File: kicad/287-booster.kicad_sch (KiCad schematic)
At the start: 4 parts

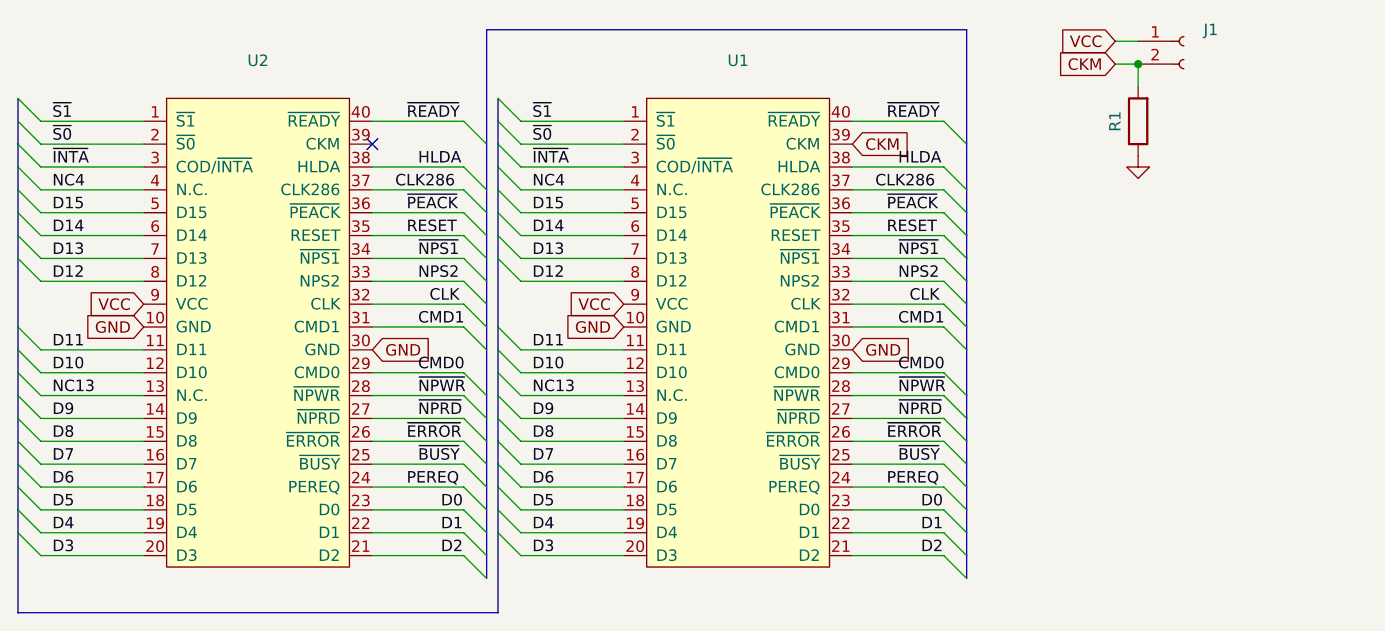
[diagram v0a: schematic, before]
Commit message: Switched to KiCad 7
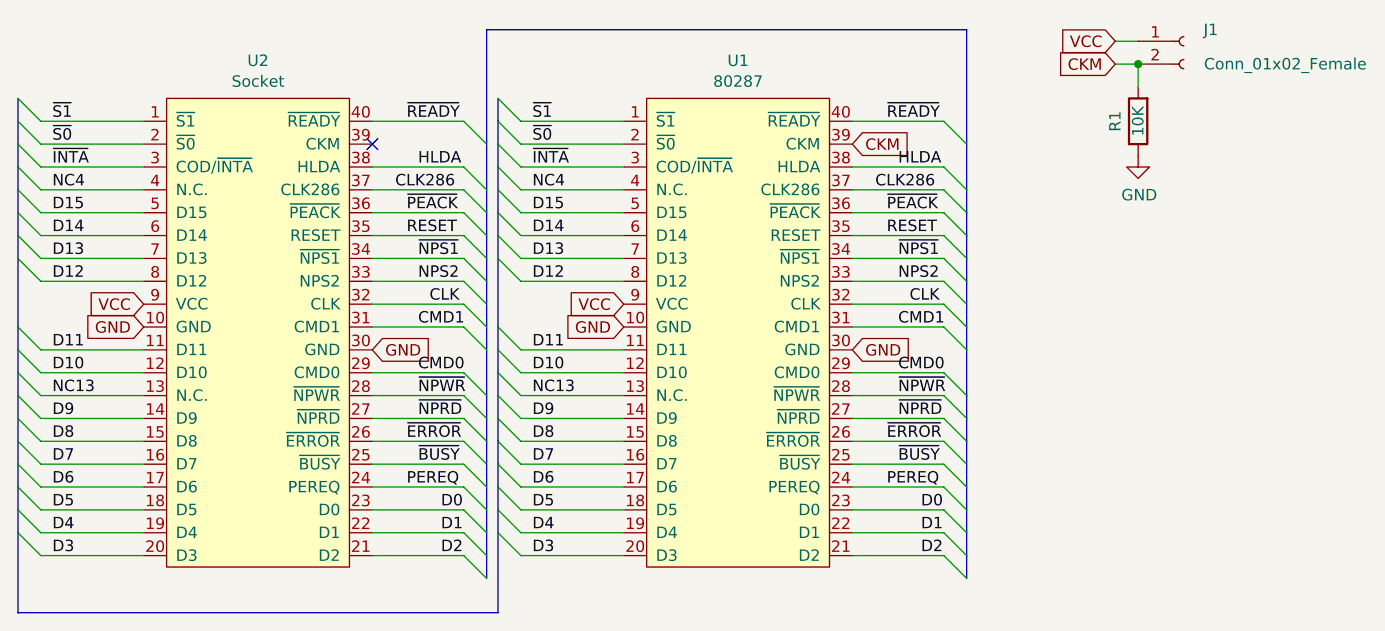
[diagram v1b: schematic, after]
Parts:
- J1: value (none) -> Conn_01x02_Female; footprint (none) -> Connector_PinHeader_2.54mm:PinHeader_1x02_P2.54mm_Vertical
- R1: value (none) -> 10K; footprint (none) -> Resistor_THT:R_Axial_DIN0207_L6.3mm_D2.5mm_P7.62mm_Horizontal
- U1: value (none) -> 80287; footprint (none) -> Package_DIP:DIP-40_W15.24mm_Socket
- U2: value (none) -> Socket; footprint (none) -> Package_DIP:DIP-40_W15.24mm
